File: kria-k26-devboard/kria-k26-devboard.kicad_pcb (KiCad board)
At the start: 8 copper layers, 121.5 x 89.8 mm, 132 parts, among them IC1 TPS2378DDA, J1 WE-RJ45_7499111121A, J2 USB4105-GF-A, J3 DC_SOCKET, J4 48393-0001, J5 48393-0001, J6 685119134923_, J7 WE_68715014022, M1 XILINX-KRIA-K26, Q1 PJA3441, U1 FT4232HPQ, U10 AP62301WU-7, U11 AP62301WU-7, U12 LTC4358CDE, U13 LTC4358CDE, U14 LTC4358CDE, U2 AP62301WU-7, U3 MAX5984AETI+T, U4 AP62301WU-7, U5 AP62301WU-7, U6 AP62301WU-7, U7 AP62301WU-7, U8 RPX-4.0-R, U9 AP62301WU-7

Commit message: Finished ETH part of the schematic
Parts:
- added C61: C_10u_0603, antmicro-footprints:0603-cap, F.Cu at (213.2, -18.4)
- added C62: C_10u_0603, antmicro-footprints:0603-cap, F.Cu at (213.2, -15.9)
- added C63: C_10n_0402, antmicro-footprints:0402-cap, F.Cu at (216.4, -16.1)
- added C64: C_10n_0402, antmicro-footprints:0402-cap, F.Cu at (220.0, -18.6)
- added C65: C_1u_0402, antmicro-footprints:0402-cap, F.Cu at (212.9, -11.7)
- added C66: C_1u_0402, antmicro-footprints:0402-cap, F.Cu at (215.8, -13.7)
- added C67: C_1u_0402, antmicro-footprints:0402-cap, F.Cu at (219.3, -16.1)
- added C68: C_1u_0402, antmicro-footprints:0402-cap, F.Cu at (222.9, -18.6)
- added C69: C_1u_0402, antmicro-footprints:0402-cap, F.Cu at (215.8, -11.7)
- added C70: C_100n_0402, antmicro-footprints:0402-cap, F.Cu at (218.7, -14.1)
- added C71: C_100n_0402, antmicro-footprints:0402-cap, F.Cu at (222.2, -16.6)
- added C72: C_100n_0402, antmicro-footprints:0402-cap, F.Cu at (212.9, -13.7)
- added C73: C_100n_0402, antmicro-footprints:0402-cap, F.Cu at (218.7, -12.1)
- added C74: C_100n_0402, antmicro-footprints:0402-cap, F.Cu at (221.6, -14.1)
- added C75: C_100n_0402, antmicro-footprints:0402-cap, F.Cu at (225.1, -16.6)
- added C76: C_100n_0402, antmicro-footprints:0402-cap, F.Cu at (221.6, -12.1)
- added C77: C_100n_0402, antmicro-footprints:0402-cap, F.Cu at (224.5, -14.6)
- added C78: C_100n_0402, antmicro-footprints:0402-cap, F.Cu at (224.5, -12.6)
- added C79: C_1u_0402, antmicro-footprints:0402-cap, F.Cu at (227.4, -14.6)
- added C80: C_1u_0402, antmicro-footprints:0402-cap, F.Cu at (224.5, -10.6)
- added C81: C_1u_0402, antmicro-footprints:0402-cap, F.Cu at (227.4, -12.6)
- added C82: C_1u_0402, antmicro-footprints:0402-cap, F.Cu at (227.4, -10.6)
- added C83: C_10n_0402, antmicro-footprints:0402-cap, F.Cu at (225.8, -18.6)
- added C84: C_10u_0603, antmicro-footprints:0603-cap, F.Cu at (216.7, -18.4)
- added J8: 5-2337992-8, antmicro-footprints:5-2337992-8, F.Cu at (177.2, -18.3)
- added U15: DP83867CRRGZR, antmicro-footprints:Texas-VQFN-48, F.Cu at (120.5, 91.0)
- J1: value WE-RJ45_7499111121A -> 5-2337992-8; footprint antmicro-footprints:7499111121A -> antmicro-footprints:5-2337992-8
- moved J1 165.8 mm to (157.7, -18.3)
- moved U11 11.8 mm to (3.42, 71.5)
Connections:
- J_SOM240_1 pad A42: /Xilinx K26 SOM/MIO73 -> /Ethernet/MIO73
- J_SOM240_1 pad A43: /Xilinx K26 SOM/MIO74 -> /Ethernet/MIO74
- J_SOM240_1 pad A44: /Xilinx K26 SOM/MIO75 -> /Ethernet/MIO75
- J_SOM240_1 pad B44: /Xilinx K26 SOM/MIO70 -> /Ethernet/MIO70
- J_SOM240_1 pad B45: /Xilinx K26 SOM/MIO71 -> /Ethernet/MIO71
- J_SOM240_1 pad B46: /Xilinx K26 SOM/MIO72 -> /Ethernet/MIO72
- J_SOM240_1 pad C42: /Xilinx K26 SOM/MIO67 -> /Ethernet/MIO67
- J_SOM240_1 pad C43: /Xilinx K26 SOM/MIO68 -> /Ethernet/MIO68
- J_SOM240_1 pad C44: /Xilinx K26 SOM/MIO69 -> /Ethernet/MIO69
- J_SOM240_1 pad D40: /Xilinx K26 SOM/MIO64 -> /Ethernet/MIO64
- J_SOM240_1 pad D41: /Xilinx K26 SOM/MIO65 -> /Ethernet/MIO65
- J_SOM240_1 pad D42: /Xilinx K26 SOM/MIO66 -> /Ethernet/MIO66
- U3 pad 15: Net-(U3-Pad15) -> /Power Supply/PoE/VSS_POE_IN
- U3 pad 17: Net-(U3-Pad15) -> /Power Supply/PoE/VSS_POE_IN
- U3 pad 19: Net-(U3-Pad15) -> /Power Supply/PoE/VSS_POE_IN

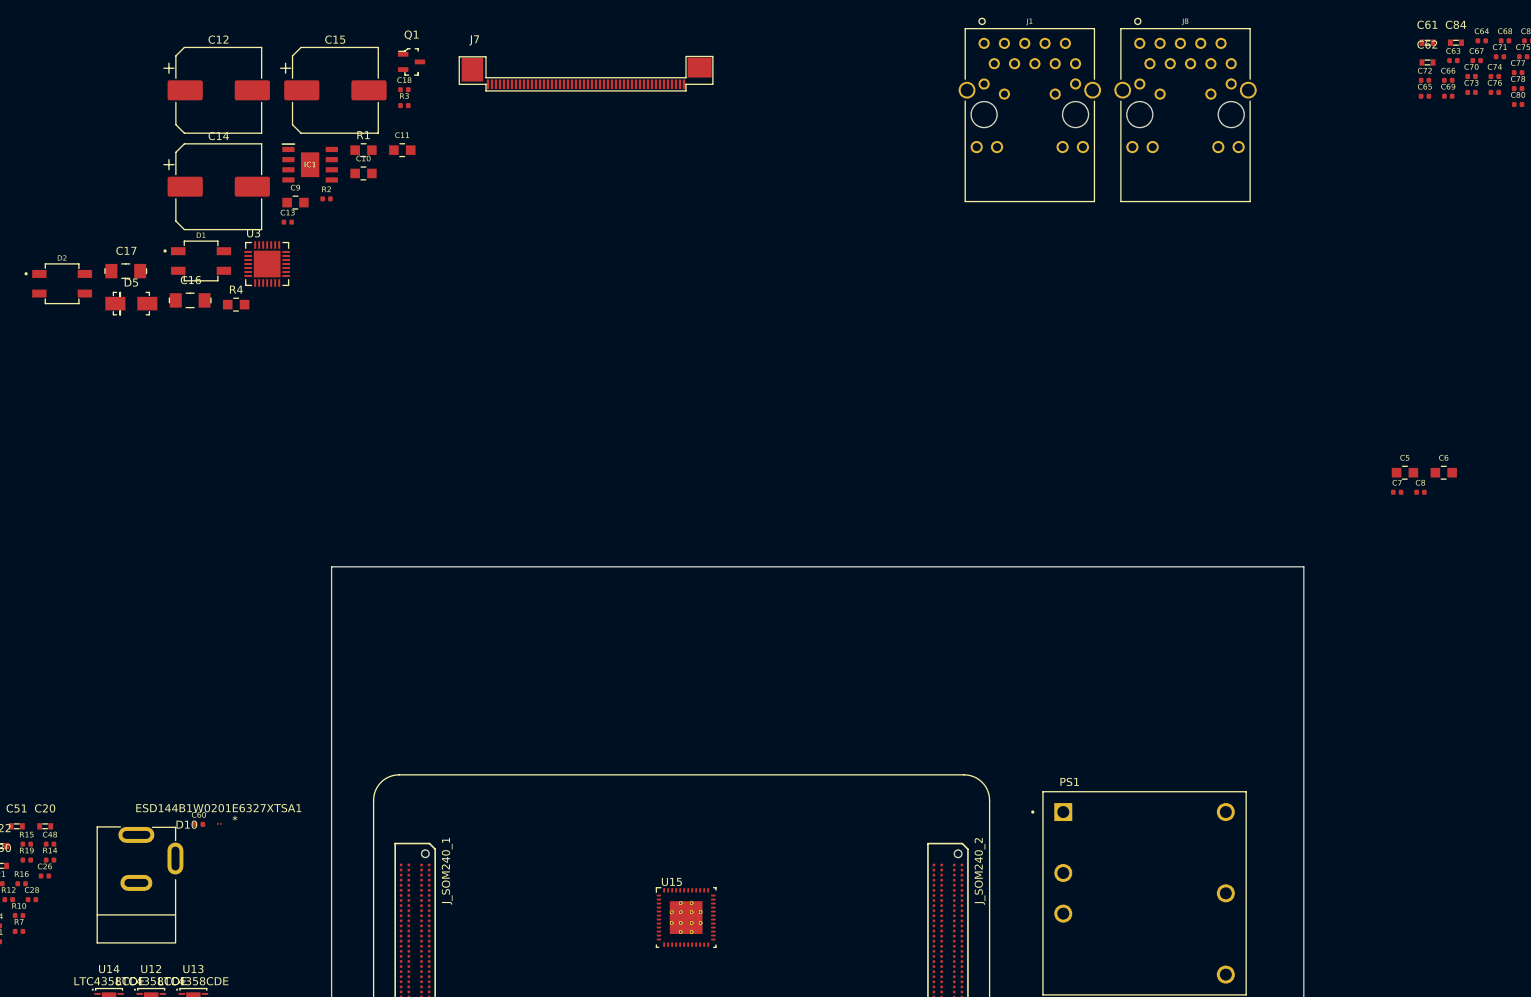
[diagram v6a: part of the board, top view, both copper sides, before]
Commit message: Added and connected USB PHY and HUB, created schematic sheet for PCIE M2 key E
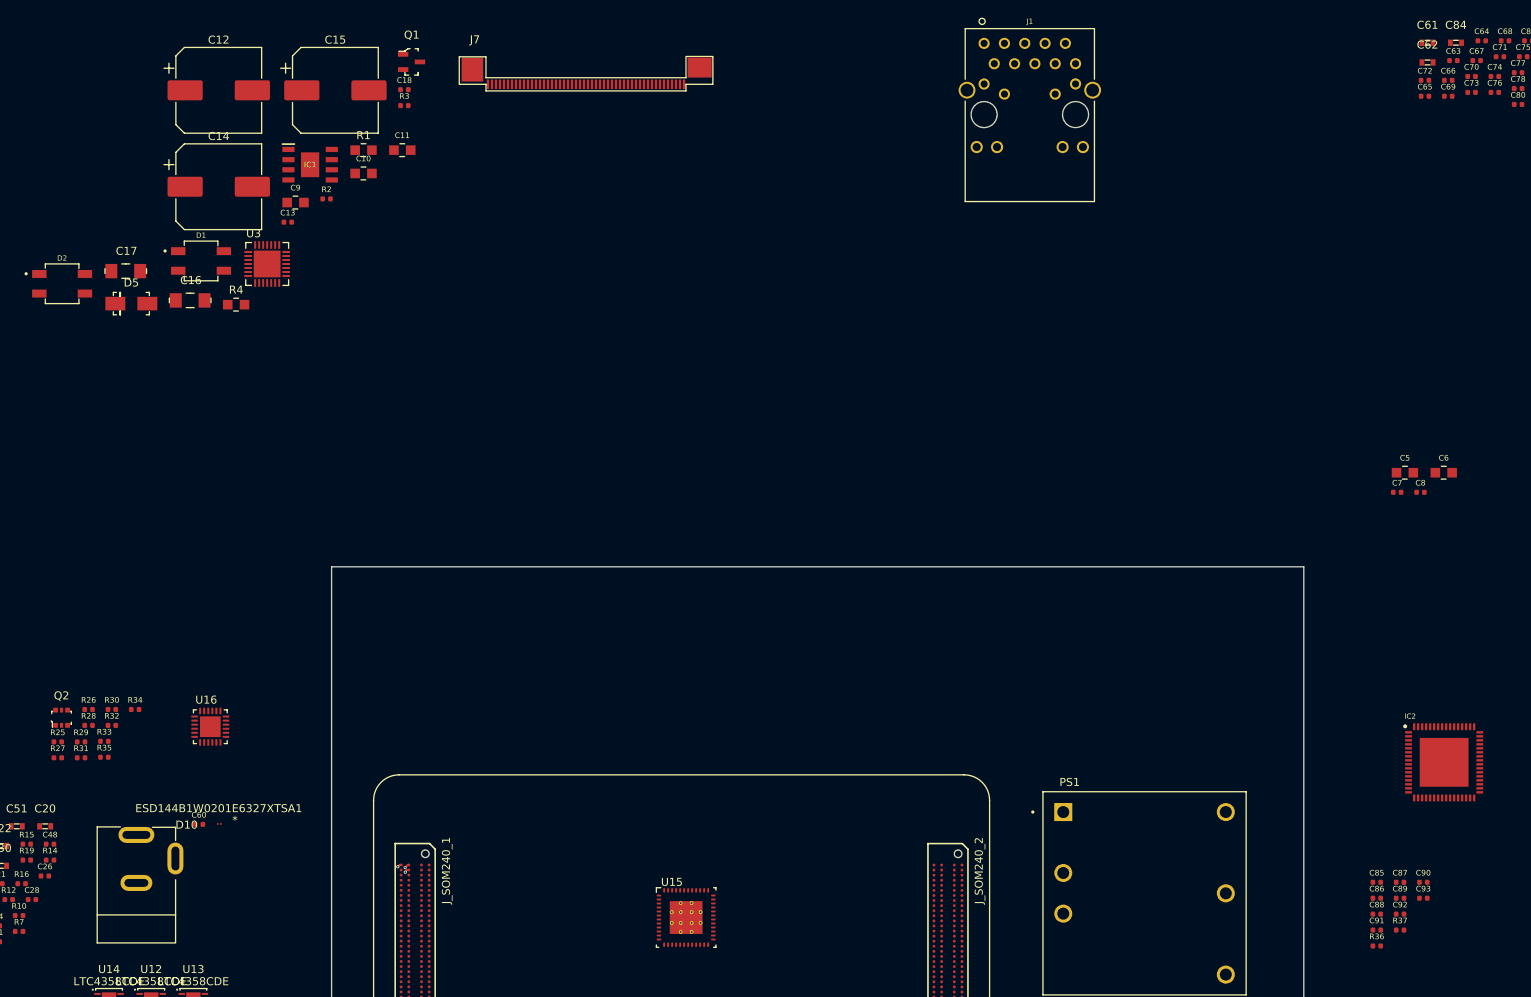
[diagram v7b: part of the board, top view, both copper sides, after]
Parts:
- removed J8: 5-2337992-8, antmicro-footprints:5-2337992-8
- added C85: C_100n_0402, antmicro-footprints:0402-cap, F.Cu at (206.8, 86.6)
- added C86: C_100n_0402, antmicro-footprints:0402-cap, F.Cu at (206.8, 88.6)
- added C87: C_100n_0402, antmicro-footprints:0402-cap, F.Cu at (209.7, 86.6)
- added C88: C_2u2_0402, antmicro-footprints:0402-cap, F.Cu at (206.8, 90.6)
- added C89: C_100n_0402, antmicro-footprints:0402-cap, F.Cu at (209.7, 88.6)
- added C90: C_100n_0402, antmicro-footprints:0402-cap, F.Cu at (212.7, 86.6)
- added C91: C_100n_0402, antmicro-footprints:0402-cap, F.Cu at (206.8, 92.6)
- added C92: C_100n_0402, antmicro-footprints:0402-cap, F.Cu at (209.7, 90.6)
- added C93: C_100n_0402, antmicro-footprints:0402-cap, F.Cu at (212.7, 88.6)
- added IC2: USB5534B-5000JZX, antmicro-footprints:USB5534B-5000JZX, F.Cu at (215.2, 71.6)
- added Q2: BSS138DW-7-F, antmicro-footprints:SOT-363, F.Cu at (42.4, 66.0)
- added R25: R_5k76_0402, antmicro-footprints:0402-res, F.Cu at (42.0, 69.0)
- added R26: R_2k49_0402, antmicro-footprints:0402-res, F.Cu at (45.8, 65.0)
- added R27: R_10k_0402, antmicro-footprints:0402-res, F.Cu at (42.0, 71.0)
- added R28: R_2k2_0402, antmicro-footprints:0402-res, F.Cu at (45.8, 67.0)
- added R29: R_11k_0402, antmicro-footprints:0402-res, F.Cu at (44.9, 69.0)
- added R30: R_4k7_0402, antmicro-footprints:0402-res, F.Cu at (48.7, 65.0)
- added R31: R_4k7_0402, antmicro-footprints:0402-res, F.Cu at (44.9, 71.0)
- added R32: R_4k7_0402, antmicro-footprints:0402-res, F.Cu at (48.7, 67.0)
- added R33: R_2k2_0402, antmicro-footprints:0402-res, F.Cu at (47.8, 69.0)
- added R34: R_330R_0402, antmicro-footprints:0402-res, F.Cu at (51.6, 65.0)
- added R35: R_330R_0402, antmicro-footprints:0402-res, F.Cu at (47.8, 71.0)
- added R36: R_10k_0402, antmicro-footprints:0402-res, F.Cu at (206.8, 94.6)
- added R37: R_8k06_0402, antmicro-footprints:0402-res, F.Cu at (209.7, 92.6)
- added U16: USB3310C-CP, antmicro-footprints:Microchip_QFN24_4X4, F.Cu at (61.0, 67.1)
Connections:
- J1 pad 19: Net-(J1-Pad19) -> GND
- J1 pad 20: Net-(J1-Pad20) -> GND
- J_SOM240_1 pad A19: /Xilinx K26 SOM/VCCOEN_PS_M2C -> /Power Supply/VCCOEN_PS_M2C
- J_SOM240_1 pad A20: /Xilinx K26 SOM/VCCO_EN_PL_M2C -> /Power Supply/VCCOEN_PL_M2C
- J_SOM240_1 pad A38: /Xilinx K26 SOM/MIO61 -> /USB/MIO61
- J_SOM240_1 pad A39: /Xilinx K26 SOM/MIO62 -> /USB/MIO62
- J_SOM240_1 pad A40: /Xilinx K26 SOM/MIO63 -> /USB/MIO63
- J_SOM240_1 pad B40: /Xilinx K26 SOM/MIO58 -> /USB/MIO58
- J_SOM240_1 pad B41: /Xilinx K26 SOM/MIO59 -> /USB/MIO59
- J_SOM240_1 pad B42: /Xilinx K26 SOM/MIO60 -> /USB/MIO60
- J_SOM240_1 pad B53: /Xilinx K26 SOM/GTR_DP2_C2M_P -> /USB/GTR_DP2_C2M_P
- J_SOM240_1 pad B54: /Xilinx K26 SOM/GTR_DP2_C2M_N -> /USB/GTR_DP2_C2M_N
- J_SOM240_1 pad C38: /Xilinx K26 SOM/MIO55 -> /USB/MIO55
- J_SOM240_1 pad C39: /Xilinx K26 SOM/MIO56 -> /USB/MIO56
- J_SOM240_1 pad C40: /Xilinx K26 SOM/MIO57 -> /USB/MIO57
- J_SOM240_1 pad D36: /Xilinx K26 SOM/MIO52 -> /USB/MIO52
- J_SOM240_1 pad D37: /Xilinx K26 SOM/MIO53 -> /USB/MIO53
- J_SOM240_1 pad D38: /Xilinx K26 SOM/MIO54 -> /USB/MIO54
- J_SOM240_1 pad D44: /Xilinx K26 SOM/MIO76 -> /Ethernet/MIO76
- J_SOM240_1 pad D45: /Xilinx K26 SOM/MIO77 -> /Ethernet/MIO77
- J_SOM240_1 pad D57: /Xilinx K26 SOM/GTR_DP2_M2C_P -> /USB/GTR_DP2_M2C_P
- J_SOM240_1 pad D58: /Xilinx K26 SOM/GTR_DP2_M2C_N -> /USB/GTR_DP2_M2C_N
- U15 pad 1: Net-(U15-Pad1) -> Net-(J1-Pad1)
- U15 pad 10: Net-(U15-Pad10) -> Net-(J1-Pad9)
- U15 pad 11: Net-(U15-Pad11) -> Net-(J1-Pad10)
- U15 pad 16: Net-(U15-Pad16) -> /Ethernet/MIO76
- U15 pad 17: Net-(U15-Pad17) -> /Ethernet/MIO77
- U15 pad 2: Net-(U15-Pad2) -> Net-(J1-Pad2)
- U15 pad 4: Net-(U15-Pad4) -> Net-(J1-Pad3)
- U15 pad 43: Net-(U15-Pad43) -> /Ethernet/ETH_RESET
- U15 pad 45: Net-(U15-Pad45) -> /Ethernet/LED2
- U15 pad 46: Net-(U15-Pad46) -> /Ethernet/LED1
- U15 pad 49: Net-(U15-Pad49) -> GND
- U15 pad 5: Net-(U15-Pad5) -> Net-(J1-Pad6)
- U15 pad 7: Net-(U15-Pad7) -> Net-(J1-Pad7)
- U15 pad 8: Net-(U15-Pad8) -> Net-(J1-Pad8)
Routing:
- net /Xilinx K26 SOM/VCC_SOM: track 0.00 -> 1.71 mm, vias 0 -> 3
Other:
- rule via_min_drill: 0.3 -> 0.2

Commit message: Updated USB sheet, finished SD 3.0 interface
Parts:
- removed J4, J5: 48393-0001, antmicro-footprints:48393-001
- added C100: C_100n_0402, antmicro-footprints:0402-cap, F.Cu at (56.2, 56.6)
- added C101: C_100n_0402, antmicro-footprints:0402-cap, F.Cu at (86.1, 31.5)
- added C102: C_100n_0402, antmicro-footprints:0402-cap, F.Cu at (74.8, 46.2)
- added C103: C_100n_0402, antmicro-footprints:0402-cap, F.Cu at (79.5, 40.8)
- added C104: C_4u7_0402, antmicro-footprints:0402-cap, F.Cu at (86.1, 33.5)
- added C105: C_4u7_0402, antmicro-footprints:0402-cap, F.Cu at (62.0, 56.6)
- added C106: C_100n_0402, antmicro-footprints:0402-cap, F.Cu at (64.9, 54.6)
- added C107: C_100n_0402, antmicro-footprints:0402-cap, F.Cu at (66.9, 52.6)
- added C108: C_100n_0402, antmicro-footprints:0402-cap, F.Cu at (59.1, 56.6)
- added C109: C_100n_0402, antmicro-footprints:0402-cap, F.Cu at (70.8, 48.6)
- added C110: C_100n_0402, antmicro-footprints:0402-cap, F.Cu at (50.4, 55.6)
- added C111: C_100n_0402, antmicro-footprints:0402-cap, F.Cu at (53.3, 54.7)
- added C112: C_100n_0402, antmicro-footprints:0402-cap, F.Cu at (36.5, 56.9)
- added C113: C_100n_0402, antmicro-footprints:0402-cap, F.Cu at (47.5, 53.6)
- added C114: C_18p_0402, antmicro-footprints:0402-cap, F.Cu at (36.5, 54.9)
- added C115: C_100n_0402, antmicro-footprints:0402-cap, F.Cu at (50.4, 53.6)
- added C116: C_100n_0402, antmicro-footprints:0402-cap, F.Cu at (47.5, 55.6)
- added C117: C_18p_0402, antmicro-footprints:0402-cap, F.Cu at (54.9, 52.7)
- added C118: C_100n_0402, antmicro-footprints:0402-cap, F.Cu at (58.2, 48.6)
- added C119: C_100n_0402, antmicro-footprints:0402-cap, F.Cu at (67.9, 50.6)
- added C120: C_100n_0402, antmicro-footprints:0402-cap, F.Cu at (67.9, 54.6)
- added C121: C_100n_0402, antmicro-footprints:0402-cap, F.Cu at (69.8, 52.6)
- added C94: C_100n_0402, antmicro-footprints:0402-cap, F.Cu at (64.0, 52.6)
- added C95: C_100n_0402, antmicro-footprints:0402-cap, F.Cu at (59.1, 54.6)
- added C96: C_100n_0402, antmicro-footprints:0402-cap, F.Cu at (56.2, 54.7)
- added C97: C_100n_0402, antmicro-footprints:0402-cap, F.Cu at (59.1, 50.6)
- added C98: C_4u7_0402, antmicro-footprints:0402-cap, F.Cu at (79.5, 38.8)
- added C99: C_4u7_0402, antmicro-footprints:0402-cap, F.Cu at (53.3, 56.6)
- added D11: PESD2USB5UV-TR, antmicro-footprints:SOT-23s, F.Cu at (75.7, 40.3)
- added D12: PESD2USB5UV-TR, antmicro-footprints:SOT-23s, F.Cu at (46.4, 50.1)
- added D13: PESD2USB5UV-TR, antmicro-footprints:SOT-23s, F.Cu at (40.4, 54.5)
- added D14: PESD2USB5UV-TR, antmicro-footprints:SOT-23s, F.Cu at (51.1, 50.1)
- added P1: 2199119-6, antmicro-footprints:TE_1-2199119-6, F.Cu at (137.3, 59.6)
- added R38: R_12k_0402, antmicro-footprints:0402-res, F.Cu at (86.1, 35.5)
- added R39: R_10k_0402, antmicro-footprints:0402-res, F.Cu at (64.9, 56.6)
- added R40: R_330R_0402, antmicro-footprints:0402-res, F.Cu at (70.8, 50.6)
- added R41: R_330R_0402, antmicro-footprints:0402-res, F.Cu at (78.4, 43.7)
- added U17: TPD4E05U06QDQARQ1, antmicro-footprints:TPD4E05U06QDQARQ1, F.Cu at (33.6, 55.9)
- added U18: TPD4E05U06QDQARQ1, antmicro-footprints:TPD4E05U06QDQARQ1, F.Cu at (86.5, 28.5)
- added U19: GSB3112311HR, antmicro-footprints:GSB3112311HR, F.Cu at (32.5, 36.9)
- added U20: TPD4E05U06QDQARQ1, antmicro-footprints:TPD4E05U06QDQARQ1, F.Cu at (55.2, 49.6)
- added U21: TPD4E05U06QDQARQ1, antmicro-footprints:TPD4E05U06QDQARQ1, F.Cu at (44.6, 54.6)
- added U22: GSB3112311HR, antmicro-footprints:GSB3112311HR, F.Cu at (53.3, 36.9)
- added U23: NVT4858HKZ, antmicro-footprints:SOT1161-2, F.Cu at (98.5, 19.0)
- added Y1: ABM8G-25.000MHZ-18-D2Y-T, antmicro-footprints:KX-7, F.Cu at (41.4, 49.8)
- C92: value C_100n_0402 -> C_1u_0402
- C93: value C_100n_0402 -> C_10u_0603; footprint antmicro-footprints:0402-cap -> antmicro-footprints:0603-cap
- moved J6 184.2 mm to (144.8, 45.6)
- moved SP4 173.4 mm to (145.9, 27.6)
- moved PS1 156.9 mm to (46.4, 2.28)
- moved C90 154.0 mm to (62.0, 54.6)
- moved C91 154.0 mm to (58.2, 52.6)
- moved C92 153.4 mm to (61.1, 52.6)
- moved U12 152.4 mm to (178.4, 14.5)
- moved C57 150.5 mm to (175.4, 18.3)
- moved C58 150.5 mm to (172.5, 18.3)
- moved R24 150.5 mm to (169.6, 18.3)
- moved C88 150.2 mm to (62.0, 50.6)
- moved C85 149.7 mm to (62.0, 48.6)
- moved C89 149.7 mm to (64.9, 50.6)
- moved C55 148.1 mm to (178.3, 18.3)
- moved U14 148.1 mm to (167.9, 14.5)
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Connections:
- C92 pad 1: /USB/GTR_DP2_M2C_C_P -> PS_3V3
- C92 pad 2: /USB/GTR_DP2_M2C_P -> Net-(C106-Pad2)
- C93 pad 1: /USB/GTR_DP2_M2C_C_N -> PS_1V2
- C93 pad 2: /USB/GTR_DP2_M2C_N -> Net-(C107-Pad2)
- IC2 pad 1: Net-(IC2-Pad1) -> /USB/USB1_P
- IC2 pad 10: Net-(IC2-Pad10) -> /USB/USB2_N
- IC2 pad 11: Net-(IC2-Pad11) -> /USB/USB2_TX_P
- IC2 pad 12: Net-(IC2-Pad12) -> /USB/USB2_TX_N
- IC2 pad 13: Net-(IC2-Pad13) -> PS_1V2
- IC2 pad 14: Net-(IC2-Pad14) -> /USB/USB2_RX_P
- IC2 pad 15: Net-(IC2-Pad15) -> /USB/USB2_RX_N
- IC2 pad 16: Net-(IC2-Pad16) -> PS_3V3
- IC2 pad 17: Net-(IC2-Pad17) -> /USB/USB3_P
- IC2 pad 18: Net-(IC2-Pad18) -> /USB/USB3_N
- IC2 pad 19: Net-(IC2-Pad19) -> /USB/USB3_TX_P
- IC2 pad 2: Net-(IC2-Pad2) -> /USB/USB1_N
- IC2 pad 20: Net-(IC2-Pad20) -> /USB/USB3_TX_N
- IC2 pad 21: Net-(IC2-Pad21) -> PS_1V2
- IC2 pad 22: Net-(IC2-Pad22) -> /USB/USB3_RX_P
- IC2 pad 23: Net-(IC2-Pad23) -> /USB/USB3_RX_N
- IC2 pad 24: Net-(IC2-Pad24) -> /USB/USB4_P
- IC2 pad 25: Net-(IC2-Pad25) -> /USB/USB4_N
- IC2 pad 26: Net-(IC2-Pad26) -> /USB/USB4_TX_P
- IC2 pad 27: Net-(IC2-Pad27) -> /USB/USB4_TX_N
- IC2 pad 28: Net-(IC2-Pad28) -> PS_1V2
- IC2 pad 29: Net-(IC2-Pad29) -> /USB/USB4_RX_P
- IC2 pad 3: Net-(IC2-Pad3) -> /USB/USB1_TX_P
- IC2 pad 30: Net-(IC2-Pad30) -> /USB/USB4_RX_N
- IC2 pad 31: Net-(IC2-Pad31) -> PS_1V2
- IC2 pad 34: Net-(IC2-Pad34) -> PS_3V3
- IC2 pad 4: Net-(IC2-Pad4) -> /USB/USB1_TX_N
- IC2 pad 5: Net-(IC2-Pad5) -> PS_1V2
- IC2 pad 51: Net-(IC2-Pad51) -> PS_1V2
- IC2 pad 52: Net-(IC2-Pad52) -> PS_3V3
- IC2 pad 57: Net-(IC2-Pad57) -> PS_1V2
- IC2 pad 58: /USB/GTR_DP2_M2C_C_P -> /USB/GTR_DP2_M2C_P
- IC2 pad 59: /USB/GTR_DP2_M2C_C_N -> /USB/GTR_DP2_M2C_N
- IC2 pad 6: Net-(IC2-Pad6) -> /USB/USB1_RX_P
- IC2 pad 61: Net-(IC2-Pad61) -> /USB/XOUT
- IC2 pad 62: Net-(IC2-Pad62) -> /USB/XIN
- IC2 pad 63: Net-(IC2-Pad63) -> PS_3V3
- IC2 pad 7: Net-(IC2-Pad7) -> /USB/USB1_RX_N
- IC2 pad 8: Net-(IC2-Pad8) -> PS_1V2
- IC2 pad 9: Net-(IC2-Pad9) -> /USB/USB2_P
- R37 pad 2: Net-(R37-Pad2) -> GND
- U16 pad 24: Net-(U16-Pad24) -> Net-(R37-Pad1)
- U16 pad 25: Net-(U16-Pad25) -> GND
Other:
- net class Default: clearance 0.2 -> 0.076; trace_width 0.25 -> 0.076
- rule trace_clearance: 0.2 -> 0.076
- rule trace_min: 0.2 -> 0.076
